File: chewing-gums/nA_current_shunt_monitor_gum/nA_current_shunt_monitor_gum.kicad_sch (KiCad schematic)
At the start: 37 parts, among them IC6 INA212AIDCKR, J1 Conn_Coaxial, J2 Conn_01x03, J3 Conn_01x03, J44 Conn_02x03_Odd_Even, J6 Conn_02x01, J7 Conn_02x01, SW4 SW_SPDT, U1 TLV75801PDBV, U10 LM321, U2 ADS1219, U3 TLV75801PDBV, U4 MCP4726

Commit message: adding PCB layout for nA gum
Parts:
- renumbered R7 to R10, R23 to R11, R28 to R12, R2 to R3, R3 to R6, R6 to R7
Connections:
- net +3.3V is gone; now on net 3.3V: R7.2
- net 3V3 is gone; now on net 3.3V: CG1.A2 (3V3)
- net A3V3 is gone; now on net A3.3V: J2.1 (Pin_1)
- net 3.3V: now also C2.2
- net GND: no longer C2.2
- net V_LSL_load: no longer CG1.D1 (OUT_0)
- no-connect marks 3 -> 4
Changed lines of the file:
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@@
 		(at 265.43 52.07)
 	)
+	(no_connect
+		(at 64.77 119.38)
+	)
 	(wire
 		(pts
@@
 	(wire
 		(pts
-			(xy 64.77 119.38) (xy 71.12 119.38)
-		)
-		(stroke
-			(width 0)
-			(type default)
-		)
-	)
-	(wire
-		(pts
 			(xy 142.875 57.15) (xy 156.845 57.15)
 		)
@@
 		)
 	)
+	(label "3.3V"
+		(at 41.91 67.31 180)
+		(effects
+			(font
+				(size 1.27 1.27)
+			)
+			(justify right bottom)
+		)
+	)
 	(label "SDA"
 		(at 66.04 45.72 0)
@@
 		)
 	)
-	(label "A3V3"
+	(label "A3.3V"
 		(at 123.19 39.37 180)
 		(effects
@@
 	)
 	(label "V_LSL_load"
-		(at 67.31 119.38 0)
-		(effects
-			(font
-				(size 1.27 1.27)
-			)
-			(justify left bottom)
-		)
-	)
-	(label "V_LSL_load"
 		(at 250.19 105.41 0)
 		(effects
@@
 		)
 	)
-	(label "3V3"
+	(label "3.3V"
 		(at 39.37 104.14 180)
 		(effects
@@
 			)
 		)
-		(property "Value" "+3.3V"
+		(property "Value" "3.3V"
 			(at 210.312 68.58 0)
 			(effects
@@
 		(on_board yes)
 		(dnp no)
-		(property "Reference" "R3"
+		(property "Reference" "R6"
 			(at 132.08 49.53 0)
 			(effects
@@
 			(project "nA_current_shunt_monitor_gum"
 				(path "/011e2255-67c3-4521-8488-9162d68859bb"
-					(reference "R3")
+					(reference "R6")
 					(unit 1)
 				)
@@
 	)
 	(symbol
-		(lib_id "power:GND")
-		(at 41.91 67.31 0)
-		(unit 1)
-		(exclude_from_sim no)
-		(in_bom yes)
-		(on_board yes)
-		(dnp no)
-		(property "Reference" "#PWR027"
-			(at 41.91 73.66 0)
-			(effects
-				(font
-					(size 1.27 1.27)
-				)
-				(hide yes)
-			)
-		)
-		(property "Value" "GND"
-			(at 42.037 71.7042 0)
-			(effects
-				(font
-					(size 1.27 1.27)
-				)
-			)
-		)
-		(property "Footprint" ""
-			(at 41.91 67.31 0)
-			(effects
-				(font
-					(size 1.27 1.27)
-				)
-				(hide yes)
-			)
-		)
-		(property "Datasheet" ""
-			(at 41.91 67.31 0)
-			(effects
-				(font
-					(size 1.27 1.27)
-				)
-				(hide yes)
-			)
-		)
-		(property "Description" ""
-			(at 41.91 67.31 0)
-			(effects
-				(font
-					(size 1.27 1.27)
-				)
-				(hide yes)
-			)
-		)
-		(pin "1"
-		)
-		(instances
-			(project "nA_current_shunt_monitor_gum"
-				(path "/011e2255-67c3-4521-8488-9162d68859bb"
-					(reference "#PWR027")
-					(unit 1)
-				)
-			)
-		)
-	)
-	(symbol
 		(lib_id "Regulator_Linear:TLV75801PDBV")
 		(at 43.18 172.72 0)
@@
 		(on_board yes)
 		(dnp no)
-		(property "Reference" "R6"
+		(property "Reference" "R7"
 			(at 218.694 61.214 0)
 			(effects
@@
 			(project "nA_current_shunt_monitor_gum"
 				(path "/011e2255-67c3-4521-8488-9162d68859bb"
-					(reference "R6")
+					(reference "R7")
 					(unit 1)
 				)
@@
 		(dnp no)
 		(fields_autoplaced yes)
-		(property "Reference" "R23"
+		(property "Reference" "R11"
 			(at 165.1 104.775 0)
 			(effects
@@
 			(project "nA_current_shunt_monitor_gum"
 				(path "/011e2255-67c3-4521-8488-9162d68859bb"
-					(reference "R23")
+					(reference "R11")
 					(unit 1)
 				)
@@
 		(on_board yes)
 		(dnp no)
-		(property "Reference" "R2"
+		(property "Reference" "R3"
 			(at 118.745 56.515 0)
 			(effects
@@
 			(project "nA_current_shunt_monitor_gum"
 				(path "/011e2255-67c3-4521-8488-9162d68859bb"
-					(reference "R2")
+					(reference "R3")
 					(unit 1)
 				)
@@
 		(dnp no)
 		(fields_autoplaced yes)
-		(property "Reference" "R28"
+		(property "Reference" "R12"
 			(at 165.1 114.935 0)
 			(effects
@@
 			(project "nA_current_shunt_monitor_gum"
 				(path "/011e2255-67c3-4521-8488-9162d68859bb"
-					(reference "R28")
+					(reference "R12")
 					(unit 1)
 				)
@@
 		(on_board yes)
 		(dnp no)
-		(property "Reference" "R7"
+		(property "Reference" "R10"
 			(at 63.754 172.974 0)
 			(effects
@@
 			(project "nA_current_shunt_monitor_gum"
 				(path "/011e2255-67c3-4521-8488-9162d68859bb"
-					(reference "R7")
+					(reference "R10")
 					(unit 1)
 				)

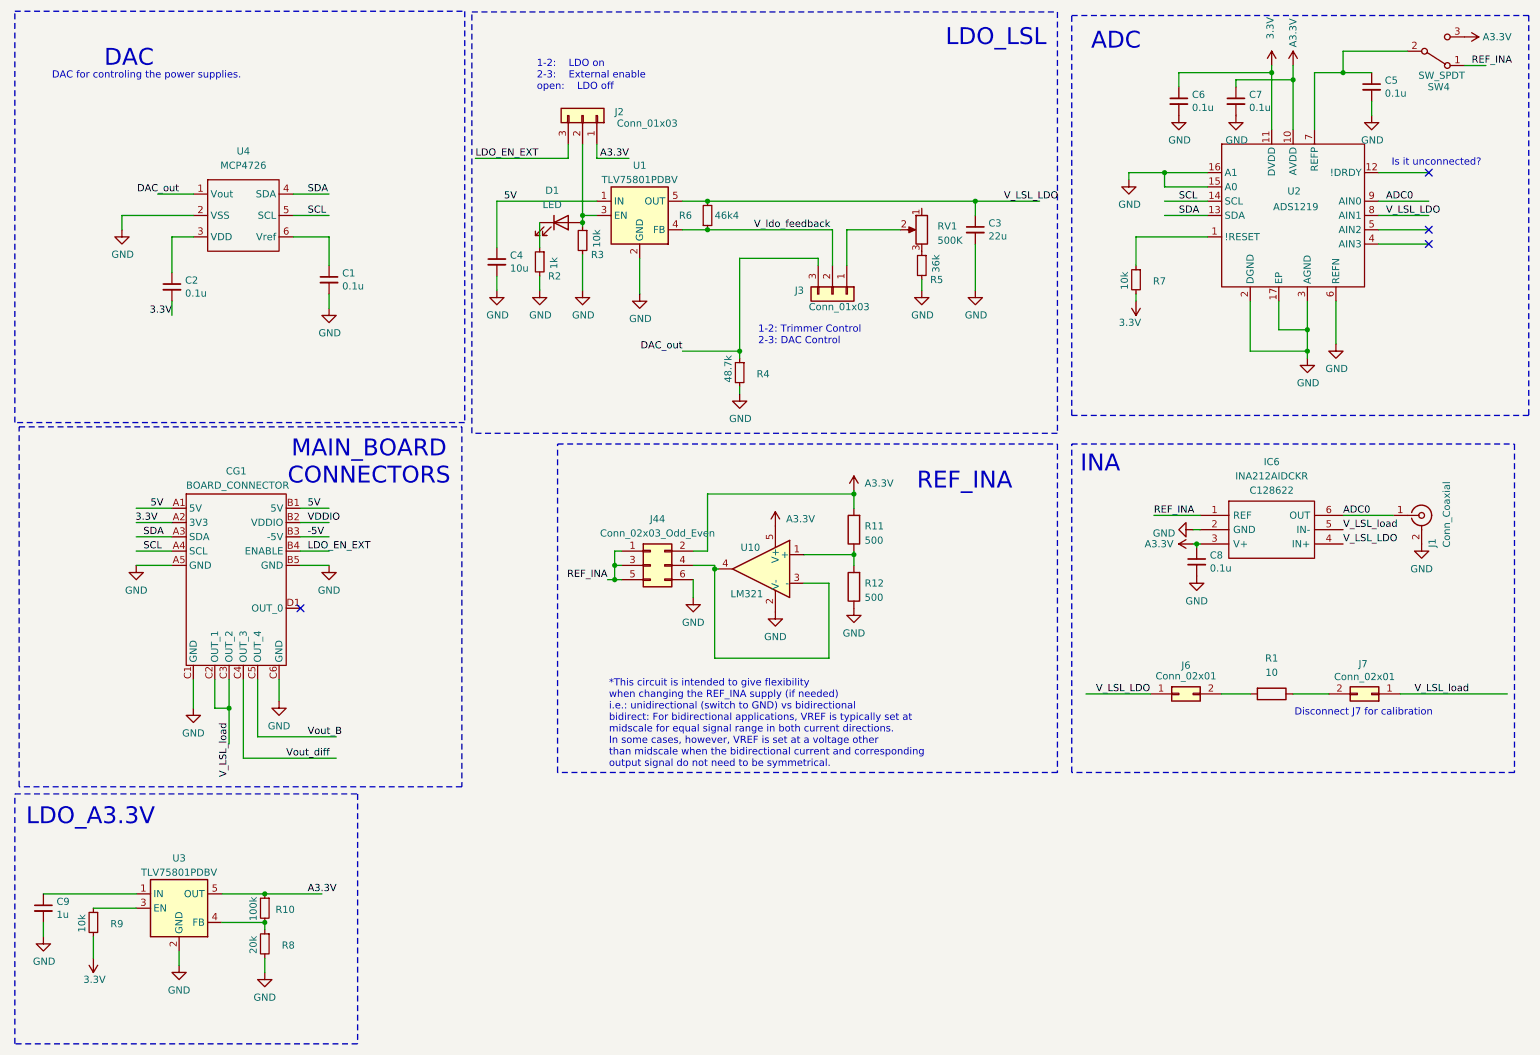
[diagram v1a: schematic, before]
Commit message: adding EEPROM in sch + fix symbol connector gum
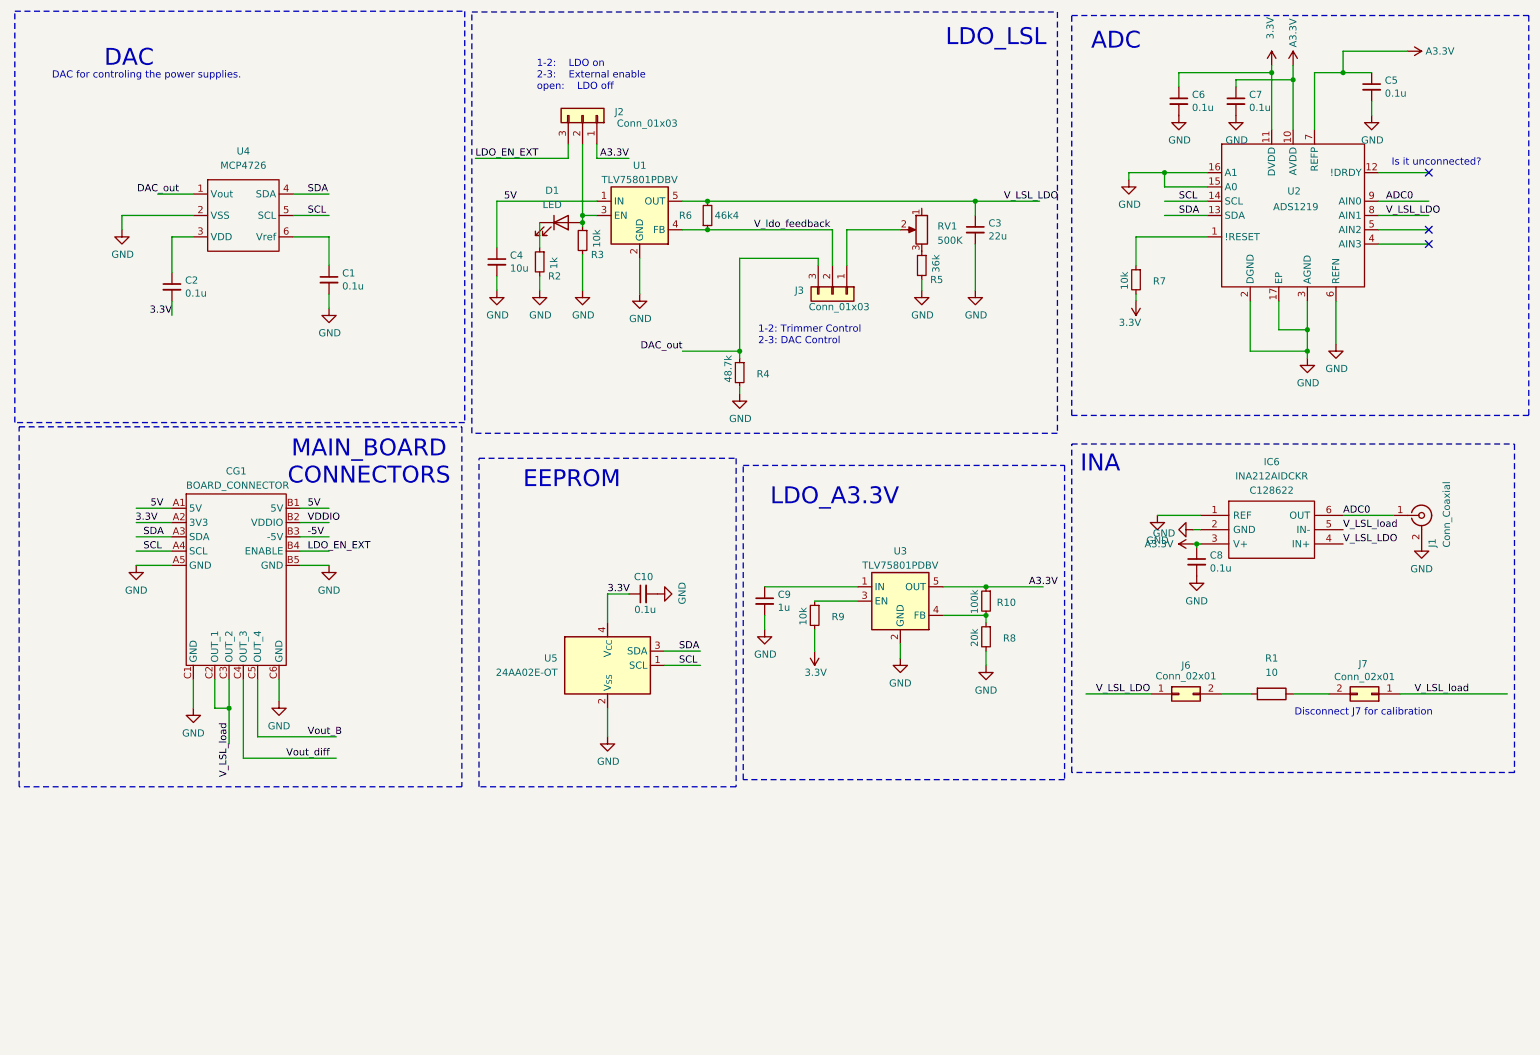
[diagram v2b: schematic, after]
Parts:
- removed J44: Conn_02x03_Odd_Even, Connector_PinSocket_2.54mm:PinSocket_2x03_P2.54mm_Vertical, symbol Connector_Generic:Conn_02x03_Odd_Even
- removed R11, R12: 500, Resistor_SMD:R_0603_1608Metric, symbol Device:R
- removed SW4: SW_SPDT, Button_Switch_SMD:SW_SPDT_PCM12, symbol Switch:SW_SPDT
- removed U10: LM321, Package_TO_SOT_SMD:SOT-23-5, symbol Amplifier_Operational:LM321
- added C10: 0.1u, Capacitor_SMD:C_0603_1608Metric, symbol Device:C_Small
- added U5: 24AA02E-OT, Package_TO_SOT_SMD:SOT-23-5, symbol Memory_EEPROM:24AA02E-OT
- CG1: symbol PCB-connectors-lib:chewing-gum -> PCB-connectors-lib:chewing-gum-board
- J1: footprint Connector_Coaxial:SMA_Amphenol_901-144_Vertical -> Connector_Coaxial:SMA_Amphenol_132289_EdgeMount
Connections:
- net REF_INA is gone; now on net GND: IC6.1 (REF)
- net 3.3V: now also C10.1, U5.4 (V_{CC})
- net A3.3V: now also C5.1, U2.7 (REFP)
- net GND: now also C10.2, U5.2 (V_{SS})
- net SCL: now also U5.1 (SCL)
- net SDA: now also U5.3 (SDA)
- no-connect marks 4 -> 3
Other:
- note added: "EEPROM"
- note removed: "*This circuit is intended to give flexibility when changing the REF_INA supply (if needed) i.e.: unidirectional (switch to GND) vs bidirectional bidirect: For bidirectional applications, VREF is typically set at midscale for equal signal range in both current directions. In some cases, however, VREF is set at a voltage other than midscale when the bidirectional current and corresponding output si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"
- note removed: "REF_INA"
- moved on the sheet: C9, R10, R8, R9, U3

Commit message: production files
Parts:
- removed J6: Conn_02x01, Connector_PinHeader_2.54mm:PinHeader_1x02_P2.54mm_Vertical, symbol Connector_Generic:Conn_02x01
- added R11: 10, Resistor_SMD:R_2010_5025Metric_Pad1.40x2.65mm_HandSolder, symbol Device:R
- added R12: 10, Resistor_SMD:R_1206_3216Metric_Pad1.30x1.75mm_HandSolder, symbol Device:R
- added R13: 1M, Resistor_SMD:R_0402_1005Metric, symbol Device:R_Small
- added R14: 10, Resistor_SMD:R_2512_6332Metric_Pad1.40x3.35mm_HandSolder, symbol Device:R
- added TP14: 5029, TestPoint:TestPoint_Keystone_5019_Miniature, symbol dk_Test-Points:5029
- added TP2: ~, TestPoint:TestPoint_Loop_D1.80mm_Drill1.0mm_Beaded, symbol Library:TP
- C1, C10, C2, C5, C6, C7, C8: LCSC C19702 -> C1590
- C3: LCSC (none) -> C84419
- C9: LCSC C19702 -> C1592
- D1: LCSC (none) -> C2286
- J2, J3: footprint Connector_PinSocket_2.54mm:PinSocket_1x03_P2.54mm_Vertical -> Connector_PinHeader_2.54mm:PinHeader_1x03_P2.54mm_Vertical
- J7: footprint Connector_PinHeader_2.54mm:PinHeader_1x02_P2.54mm_Vertical -> Connector_PinHeader_2.54mm:PinHeader_1x03_P2.54mm_Vertical; symbol Connector_Generic:Conn_02x01 -> Connector_Generic:Conn_01x03
- R1: footprint Resistor_SMD:R_0603_1608Metric -> Resistor_SMD:R_0805_2012Metric_Pad1.20x1.40mm_HandSolder; LCSC C21190 -> (none); now not fitted
- R10: LCSC C98220 -> C25803
- R2: LCSC (none) -> C21190
- R4: LCSC C98220 -> C23063
- R5: LCSC (none) -> C23147
- R6: LCSC (none) -> C23059
- R8: LCSC C98220 -> C4184
- RV1: LCSC (none) -> C83694
- U2: LCSC (none) -> C2670319
- U4: footprint Package_TO_SOT_SMD:TSOT-23-6_HandSoldering -> Package_TO_SOT_SMD:TSOT-23-6; LCSC (none) -> C191581
- U5: LCSC (none) -> C38987
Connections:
- net 3.3V: now also C2.1, U4.3 (VDD); no longer C2.2
- net 5V: now also C9.1, J2.1 (Pin_1), U3.1 (IN)
- net A3.3V: now also C1.1, U4.6 (Vref); no longer J2.1 (Pin_1)
- net GND: now also C2.2, R13.2, TP14.1
- net V_LSL_LDO: now also R1.2, R11.2, R12.2, R14.2, TP2.1
- net V_LSL_load: no longer IC6.5 (IN-)
- net Shunt-: now reaches J7.2 (Pin_2), R1.1
- net Shunt-: now also IC6.5 (IN-), R11.1, R12.1, R14.1
- new net: J7.3 (Pin_3), R13.1
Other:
- moved on the sheet: D1, J2, R2, R3, U1
